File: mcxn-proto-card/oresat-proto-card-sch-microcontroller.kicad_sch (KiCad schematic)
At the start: 101 parts, among them U1 MCXN947VKLT, U8 TCAN330, Y2 24 MHz

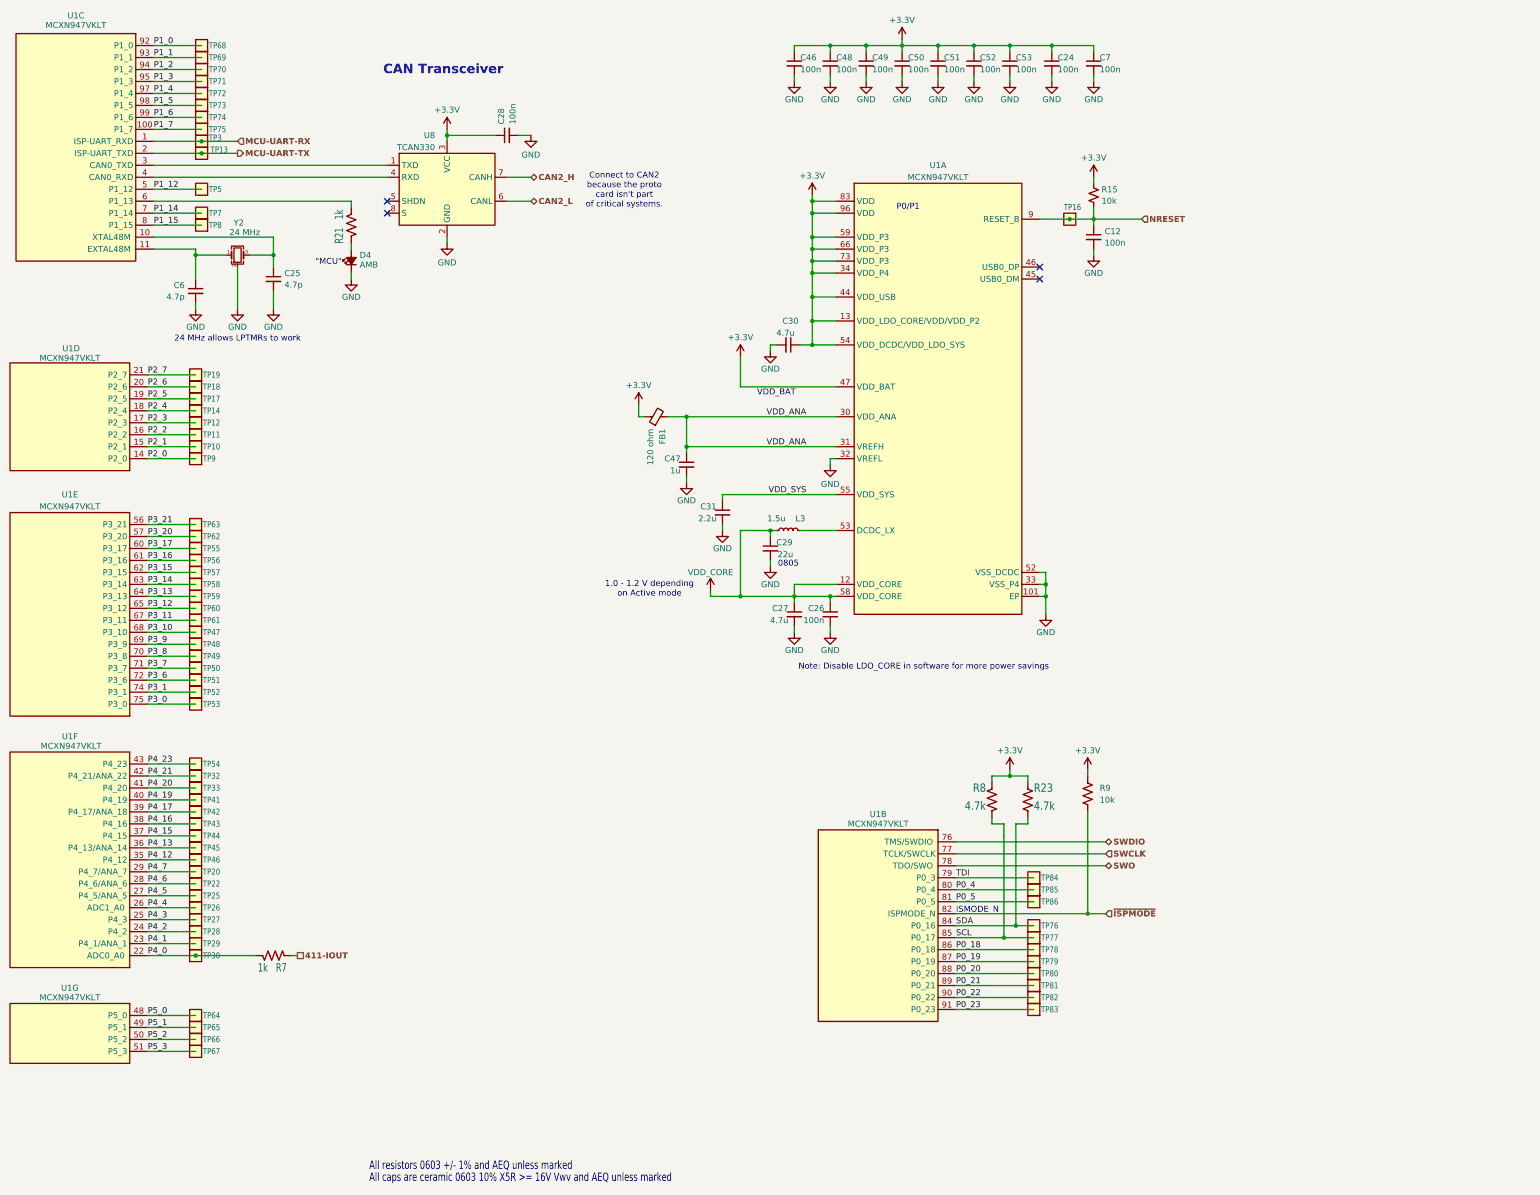
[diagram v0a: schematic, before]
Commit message: Updated BOM to match OPD writeup; Best Possible OPD now? Maybe?
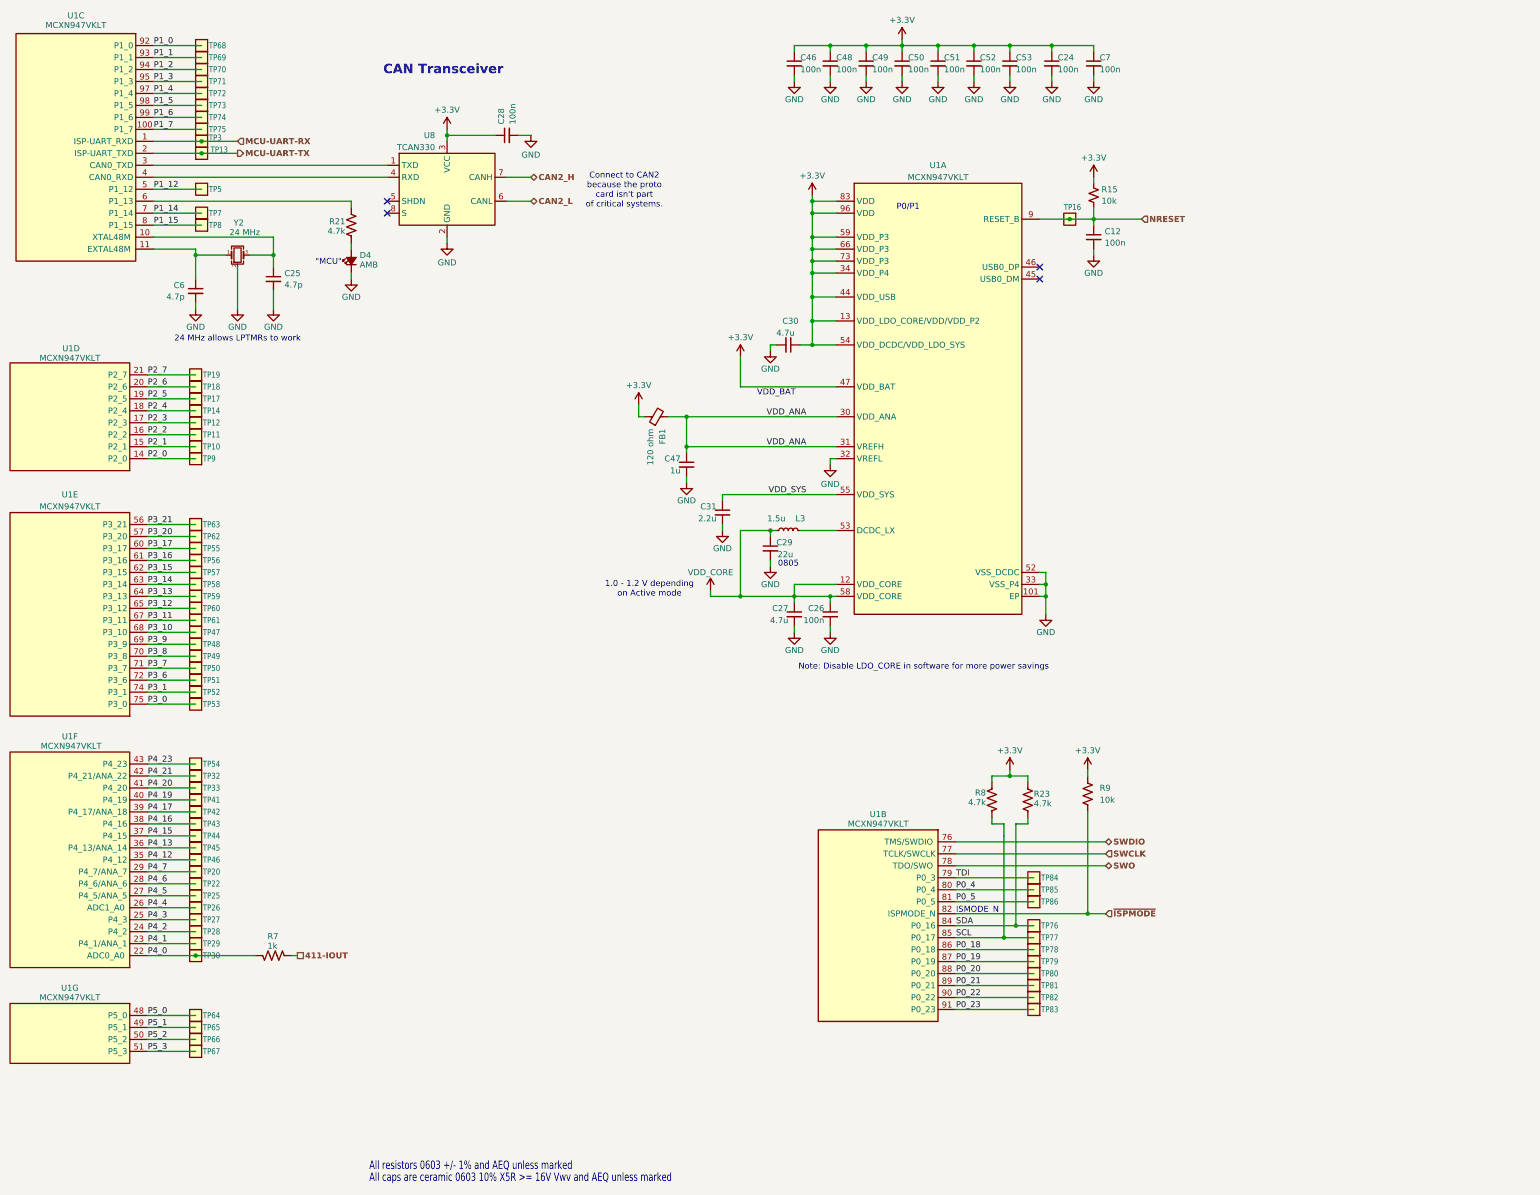
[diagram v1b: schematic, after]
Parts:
- R21: value 1k -> 4.7k; DPN RMCF0603FT1K00CT-ND -> RMCF0603FT4K70CT-ND; MPN RMCF0603FT1K00 -> RMCF0603FT4K70
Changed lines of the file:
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@@
 		(dnp no)
 		(property "Reference" "R7"
-			(at 93.218 219.964 90)
+			(at 91.44 213.614 90)
 			(show_name no)
 			(do_not_autoplace no)
 			(effects
 				(font
-					(size 1.778 1.27)
+					(size 1.27 1.27)
 				)
 				(justify right top)
@@
 		)
 		(property "Value" "1k"
-			(at 89.408 219.964 90)
+			(at 91.44 215.646 90)
 			(show_name no)
 			(do_not_autoplace no)
 			(effects
 				(font
-					(size 1.778 1.27)
+					(size 1.27 1.27)
 				)
 				(justify right top)
@@
 		(lib_id "Device:R_US")
 		(at 109.22 63.5 0)
-		(mirror y)
 		(unit 1)
 		(body_style 1)
@@
 		(dnp no)
 		(property "Reference" "R21"
-			(at 107.696 64.008 90)
+			(at 107.95 61.976 0)
 			(show_name no)
 			(do_not_autoplace no)
 			(effects
 				(font
-					(size 1.778 1.27)
+					(size 1.27 1.27)
 				)
 				(justify right top)
 			)
 		)
-		(property "Value" "1k"
-			(at 107.696 60.198 90)
+		(property "Value" "4.7k"
+			(at 107.95 64.008 0)
 			(show_name no)
 			(do_not_autoplace no)
 			(effects
 				(font
-					(size 1.778 1.27)
+					(size 1.27 1.27)
 				)
 				(justify right top)
@@
 		)
 		(property "Footprint" "oresat-passives:0603-C-NOSILK"
-			(at 108.204 63.754 90)
+			(at 110.236 63.754 90)
 			(hide yes)
 			(show_name no)
@@
 			)
 		)
-		(property "Description" "1 kOhms ±1% 0.1W, 1/10W Chip Resistor 0603 (1608 Metric) Automotive AEC-Q200 Thick Film"
+		(property "Description" "4.7 kOhms ±1% 0.1W, 1/10W Chip Resistor 0603 (1608 Metric) Automotive AEC-Q200 Thick Film"
 			(at 109.22 63.5 0)
 			(hide yes)
@@
 			)
 		)
-		(property "DPN" "RMCF0603FT1K00CT-ND"
+		(property "DPN" "RMCF0603FT4K70CT-ND"
 			(at 109.22 63.5 0)
 			(hide yes)
@@
 			)
 		)
-		(property "MPN" "RMCF0603FT1K00"
+		(property "MPN" "RMCF0603FT4K70"
 			(at 109.22 63.5 0)
 			(hide yes)
@@
 		(dnp no)
 		(property "Reference" "R8"
-			(at 243.84 182.88 0)
+			(at 243.84 183.896 0)
 			(show_name no)
 			(do_not_autoplace no)
 			(effects
 				(font
-					(size 1.778 1.5113)
+					(size 1.27 1.27)
 				)
 				(justify right)
@@
 		)
 		(property "Value" "4.7k"
-			(at 243.84 186.69 0)
+			(at 243.84 185.928 0)
 			(show_name no)
 			(do_not_autoplace no)
 			(effects
 				(font
-					(size 1.778 1.5113)
+					(size 1.27 1.27)
 				)
 				(justify right)
@@
 		(dnp no)
 		(property "Reference" "R23"
-			(at 254 182.88 0)
+			(at 254 184.15 0)
 			(show_name no)
 			(do_not_autoplace no)
 			(effects
 				(font
-					(size 1.778 1.5113)
+					(size 1.27 1.27)
 				)
 				(justify right)
@@
 		)
 		(property "Value" "4.7k"
-			(at 254 186.69 0)
+			(at 254 186.182 0)
 			(show_name no)
 			(do_not_autoplace no)
 			(effects
 				(font
-					(size 1.778 1.5113)
+					(size 1.27 1.27)
 				)
 				(justify right)

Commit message: OPD Fix
TCAN change from 330 to 337, added ISP TP, made PO_23:21 the version pins, added capacitor and resistor for OPD fix, and changed revision to 6.2
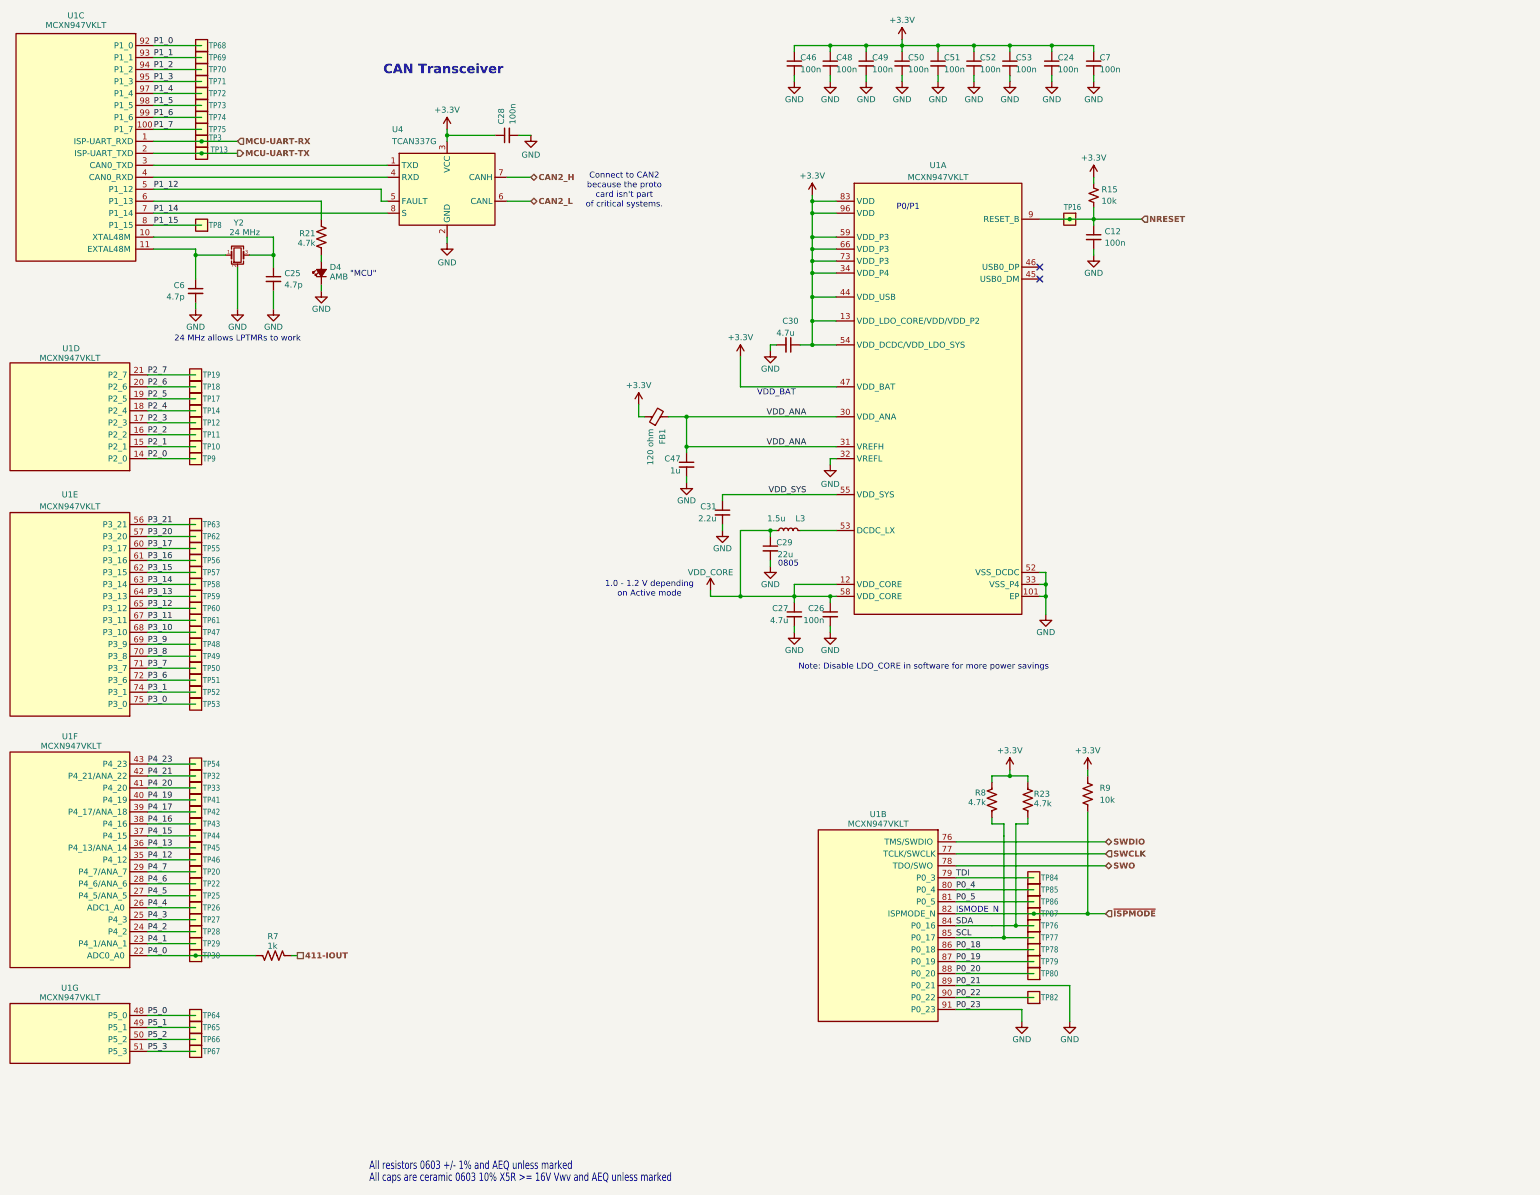
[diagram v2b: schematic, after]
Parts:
- removed TP5, TP7, TP81, TP83: Test-Point, oresat-misc:TestPoint-0.75mm-th, symbol oresat-misc:Test-Point-0.75mm-th
- removed U8: TCAN330, Package_TO_SOT_SMD:SOT-23-8, symbol Interface_CAN_LIN:TCAN330
- added TP87: Test-Point, oresat-misc:TestPoint-0.75mm-th, symbol oresat-misc:Test-Point-0.75mm-th
- added U4: TCAN337G, Package_TO_SOT_SMD:SOT-23-8, symbol Interface_CAN_LIN:TCAN337G
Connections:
- net P0_21 is gone; now on net GND: U1.89 (P0_21)
- net P0_23 is gone; now on net GND: U1.91 (P0_23)
- net +3.3V: now also U4.3 (VCC)
- net CAN2_H: now also U4.7 (CANH)
- net CAN2_L: now also U4.6 (CANL)
- net GND: now also U4.2 (GND)
- net P1_12: now also U4.5 (FAULT)
- net P1_14: now also U4.8 (S)
- net ~{ISPMODE}: now also TP87.1
- net at U1.3 (P1_10): now also U4.1 (TXD)
- net at U1.4 (P1_11): now also U4.4 (RXD)
- no-connect marks 4 -> 2
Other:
- moved on the sheet: D4, R21

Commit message: Fixed version pins and lots of ref des formatting; BOM still not right.
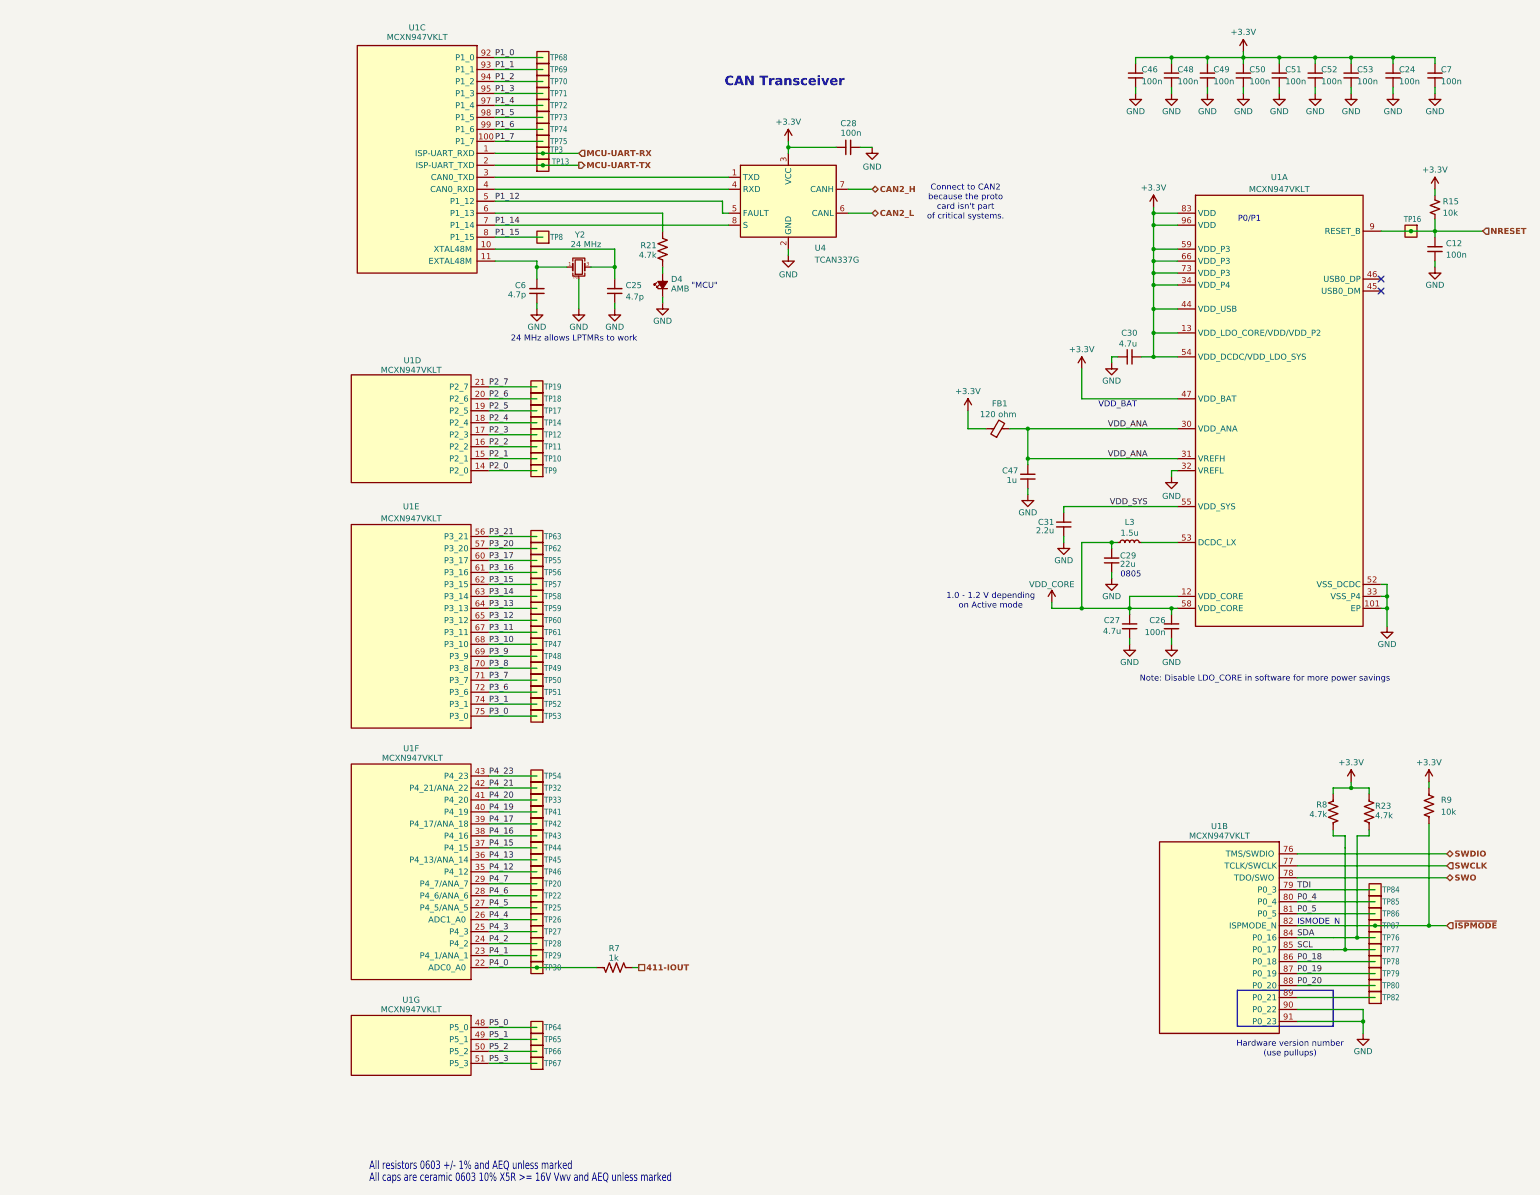
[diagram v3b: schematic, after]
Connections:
- net GND: now also U1.90 (P0_22); no longer U1.89 (P0_21)
- net P0_22: no longer names the net of TP82.1
- net P0_22: now also U1.89 (P0_21); no longer U1.90 (P0_22)
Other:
- note added: "Hardware version number (use pullups)"
- moved on the sheet: C12, C24, C25, C26, C27, C28, C29, C30, C31, C46, C47, C48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
